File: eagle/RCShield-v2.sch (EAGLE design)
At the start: 48 parts, among them J1/J2 JOYSTICKPTH, U1 TOUSCRUINO_SHIELD, U2 FT232RL-BASICSSOP, U4 XBEE, X1 USBSMD

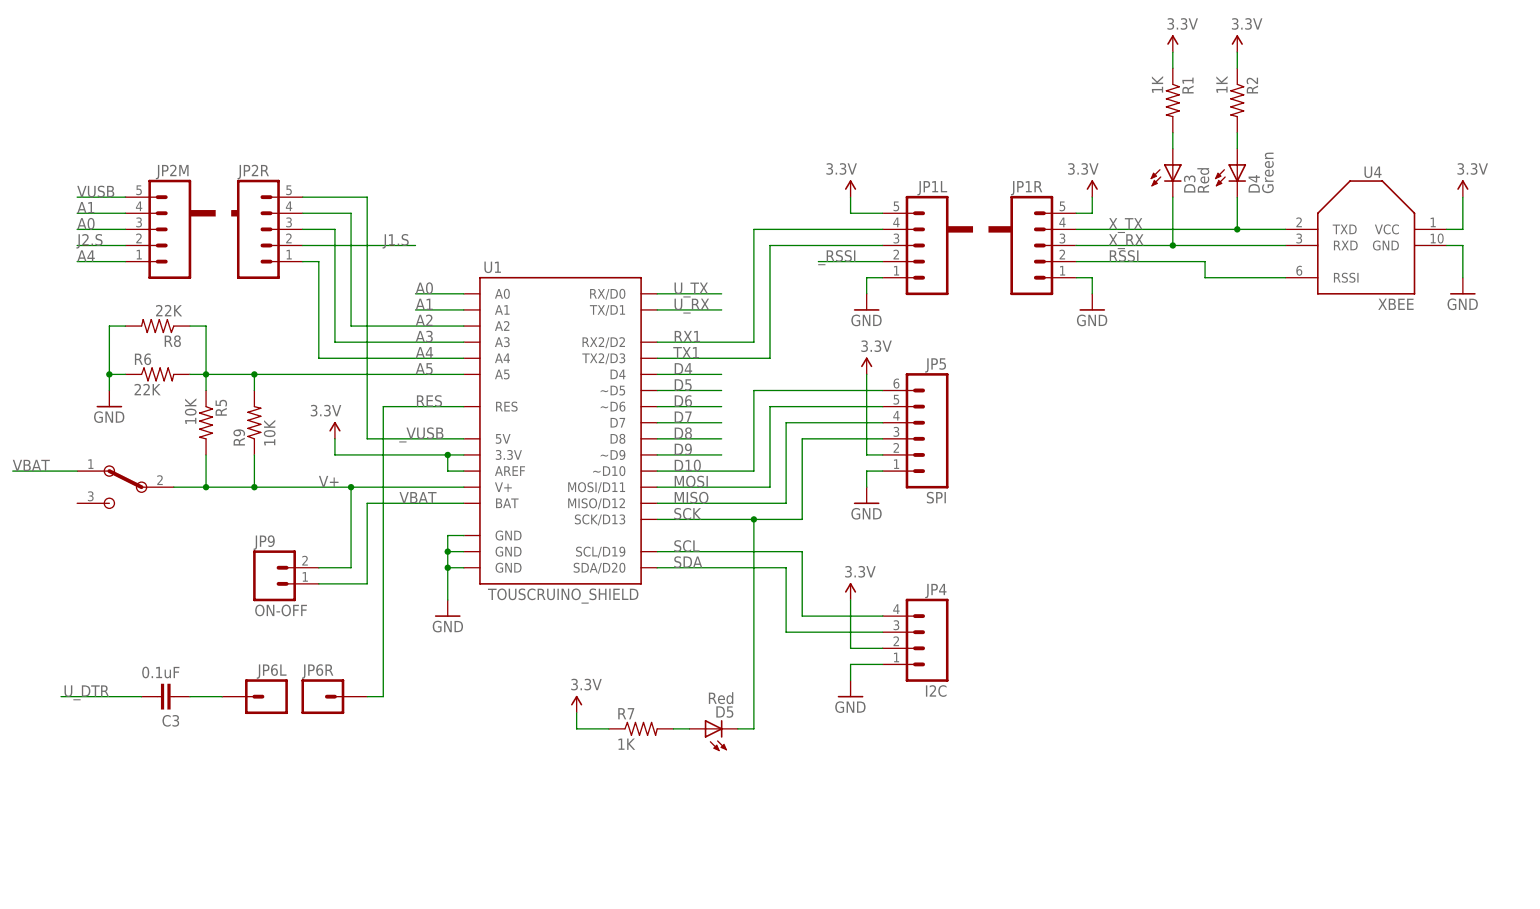
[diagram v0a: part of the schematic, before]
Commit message: 
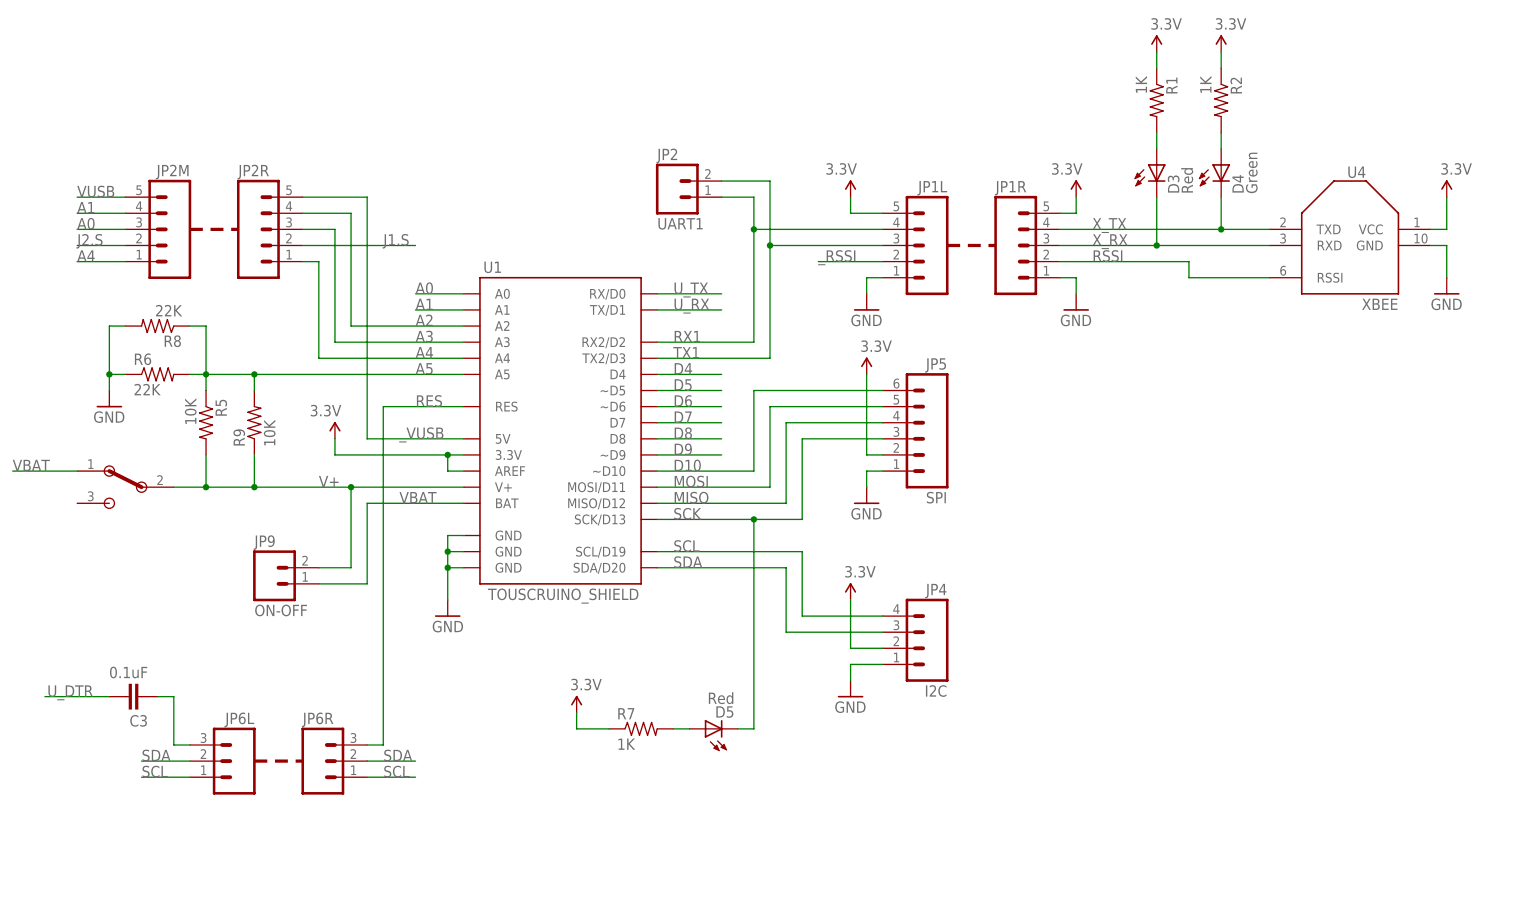
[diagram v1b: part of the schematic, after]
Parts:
- added JP2: UART1, wibauxl:M02
- JP6L, JP6R: value M01PTH -> (none); device SparkFun:M01PTH -> SparkFun:M03PTH
- P1/P3, P2/P4: value (none) -> POT; device SparkFun:POT -> wibauxl:POT
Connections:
- removed net N$11: C3.2, JP6L.1
- new net N$1: C3.2, JP6L.3
- net RES: now also JP6R.3; no longer JP6R.1
- net RX1: now also JP2.1
- net SCL: now also JP6L.1, JP6R.1
- net SDA: now also JP6L.2, JP6R.2
- net TX1: now also JP2.2
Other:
- moved on the sheet: C3, D3, D4, JP1R, R1, R2, U4

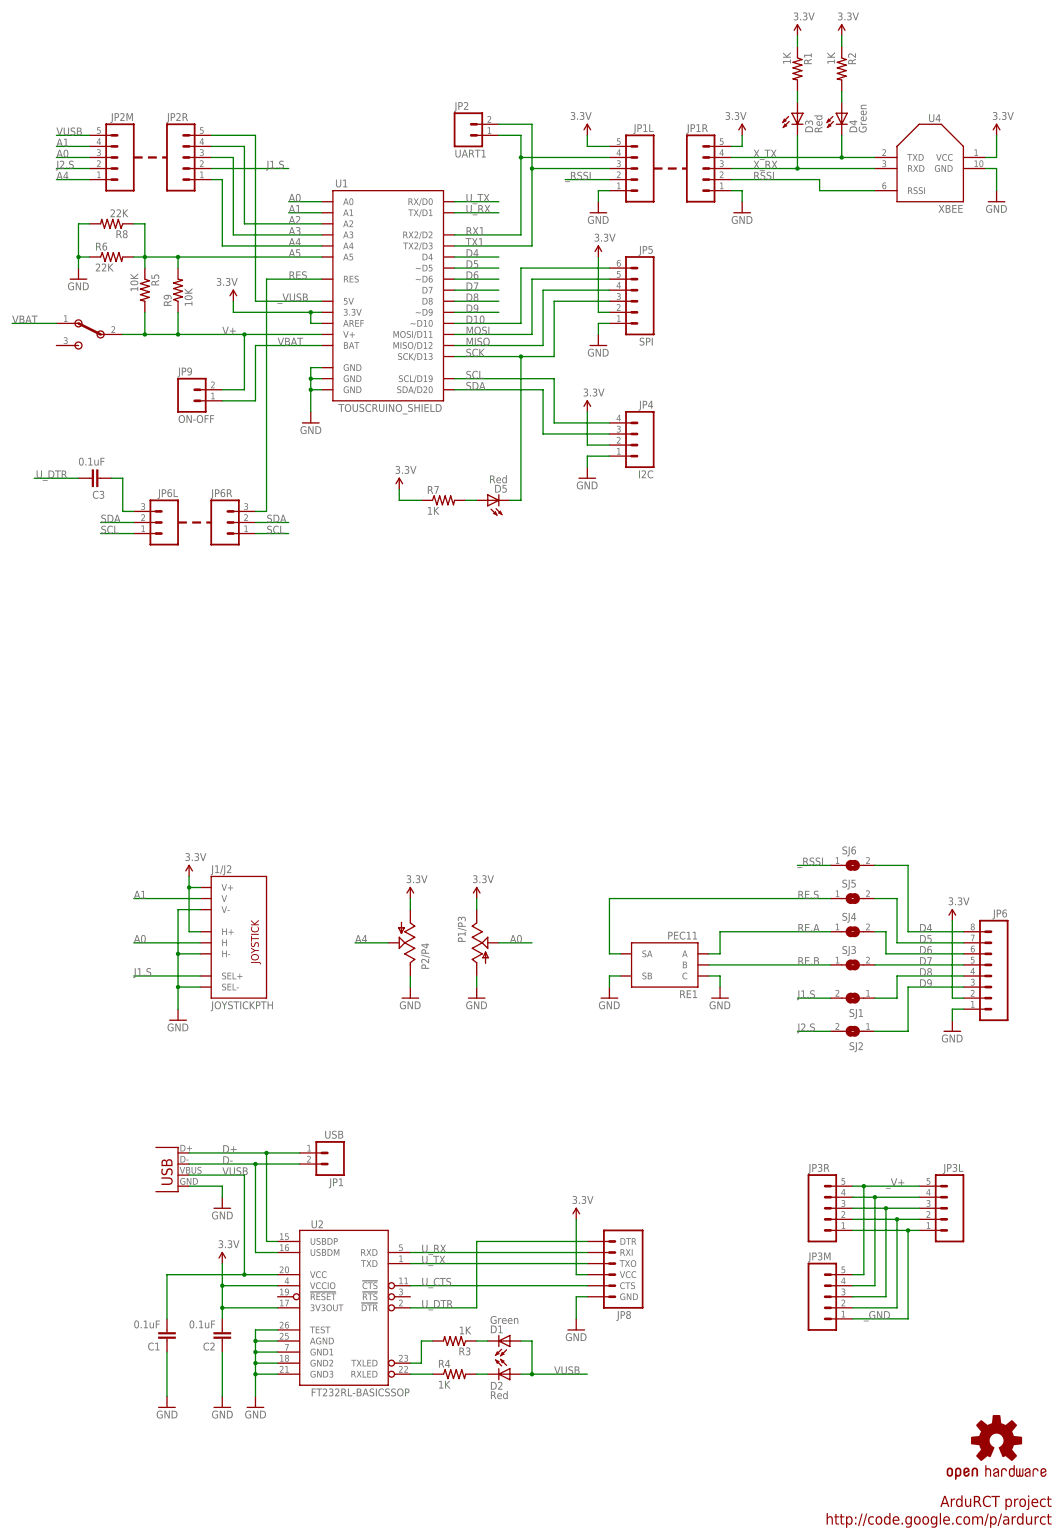
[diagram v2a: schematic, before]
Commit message: 
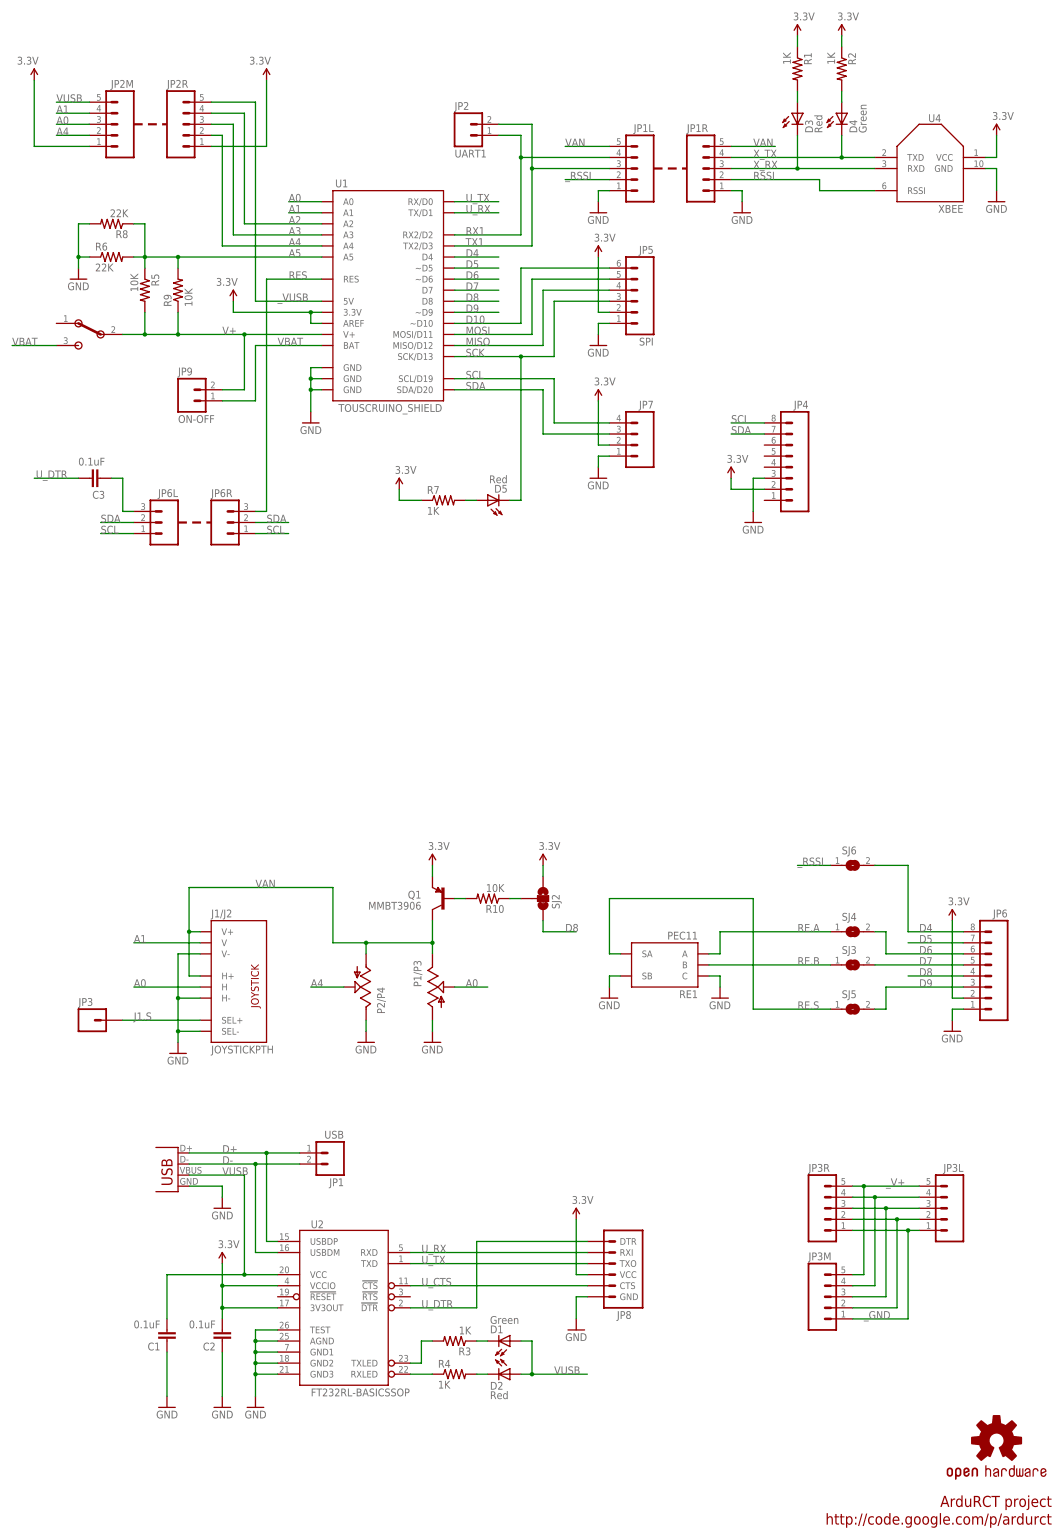
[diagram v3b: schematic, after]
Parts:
- removed SJ1: (no value), jumper:SJ
- added JP3: M01PTH, SparkFun:M01PTH
- added JP7: M04, wibauxl:M04
- added Q1: MMBT3906, wibauxl:TRANSISTOR_PNPSMD
- added R10: 10K, SparkFun:RESISTOR0805-RES
- JP4: value I2C -> M08; device wibauxl:M04 -> wibauxl:M08
- SJ2: value (none) -> SJ_2WAYS_1-2W; device jumper:SJ -> wibauxl:SJ_2WAYS_1-2W
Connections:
- removed net J2.S: JP2M.2, SJ2.2
- new net N$2: Q1.B, R10.2
- new net N$3: R10.1, SJ2.2
- new net VAN: J1/J2.H+, J1/J2.V+, JP1L.5, JP1R.5, P1/P3.E, P2/P4.A, Q1.C
- net 3.3V: now also JP2M.1, JP2R.1, JP7.2, Q1.E, SJ2.3; no longer J1/J2.H+, J1/J2.V+, JP1L.5, JP1R.5, P1/P3.E, P2/P4.A
- net A4: now also JP2M.2, JP2R.2; no longer JP2M.1, JP2R.1
- net D5: no longer SJ5.2
- net D8: now also SJ2.1; no longer SJ1.1
- net D9: now also SJ5.2; no longer SJ2.1
- net GND: now also JP4.3, JP7.1; no longer JP4.1
- net J1.S: now also JP3.1; no longer JP2R.2, SJ1.2
- net SCL: now also JP4.8, JP7.4; no longer JP4.4
- net SDA: now also JP4.7, JP7.3; no longer JP4.3
- net VBAT: now also S4.3; no longer S4.1
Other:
- moved on the sheet: J1/J2, JP2M, JP2R, P1/P3, P2/P4, SJ5

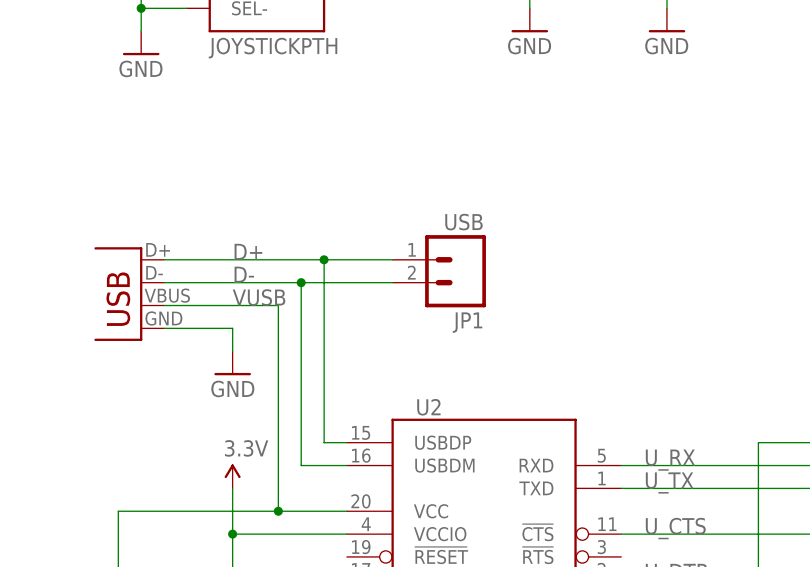
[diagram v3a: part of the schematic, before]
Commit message: 
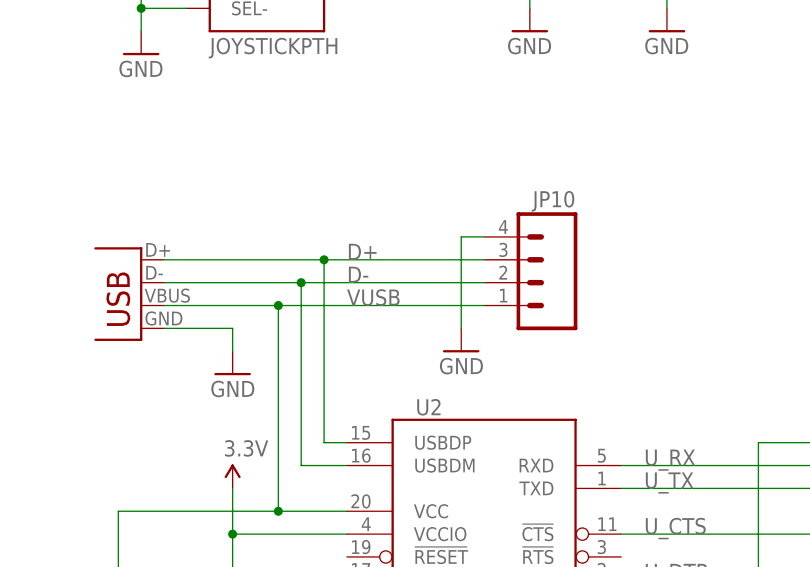
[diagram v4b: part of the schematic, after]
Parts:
- removed JP1: USB, wibauxl:M02
- added JP10: M04, wibauxl:M04
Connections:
- net D+: now also JP10.3; no longer JP1.1
- net D-: now also JP10.2; no longer JP1.2
- net GND: now also JP10.4
- net VUSB: now also JP10.1
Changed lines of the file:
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@@
 <part name="R9" library="resistor" deviceset="R-US_" device="0207/7" value="10K"/>
 <part name="P+15" library="SparkFun" deviceset="3.3V" device=""/>
-<part name="JP1" library="wibauxl" deviceset="M02" device="" value="USB"/>
 <part name="RE1" library="wibauxl" deviceset="PEC11" device=""/>
 <part name="U$4" library="wibauxl" deviceset="FRAME_LETTER" device=""/>
@@
 <part name="GND12" library="SparkFun" deviceset="GND" device=""/>
 <part name="P+4" library="SparkFun" deviceset="3.3V" device=""/>
+<part name="JP10" library="wibauxl" deviceset="M04" device="" value=""/>
+<part name="GND13" library="SparkFun" deviceset="GND" device=""/>
 </parts>
 <sheets>
@@
 <instance part="R9" gate="G$1" x="43.18" y="302.26" rot="R90"/>
 <instance part="P+15" gate="G$1" x="53.34" y="78.74"/>
-<instance part="JP1" gate="G$1" x="76.2" y="104.14" rot="R180"/>
 <instance part="RE1" gate="G$1" x="154.94" y="147.32" rot="MR0"/>
 <instance part="U$4" gate="G$1" x="0" y="210.82"/>
@@
 <instance part="GND12" gate="1" x="175.26" y="248.92"/>
 <instance part="P+4" gate="G$1" x="170.18" y="259.08"/>
+<instance part="JP10" gate="G$1" x="86.36" y="101.6" rot="MR0"/>
+<instance part="GND13" gate="1" x="78.74" y="93.98" rot="MR0"/>
 </instances>
 <busses>
@@
 <pinref part="GND12" gate="1" pin="GND"/>
 </segment>
+<segment>
+<pinref part="JP10" gate="G$1" pin="4"/>
+<wire x1="81.28" y1="106.68" x2="78.74" y2="106.68" width="0.1524" layer="91"/>
+<wire x1="78.74" y1="106.68" x2="78.74" y2="96.52" width="0.1524" layer="91"/>
+<pinref part="GND13" gate="1" pin="GND"/>
+</segment>
 </net>
 <net name="3.3V" class="0">
@@
 <wire x1="40.64" y1="76.2" x2="40.64" y2="66.04" width="0.1524" layer="91"/>
 <junction x="58.42" y="76.2"/>
-<label x="53.34" y="99.06" size="1.778" layer="95"/>
+<label x="66.04" y="99.06" size="1.778" layer="95"/>
 <pinref part="U2" gate="G$1" pin="VCC"/>
 <pinref part="X1" gate="G$1" pin="VBUS"/>
 <pinref part="C1" gate="G$1" pin="2"/>
+<pinref part="JP10" gate="G$1" pin="1"/>
+<wire x1="58.42" y1="99.06" x2="81.28" y2="99.06" width="0.1524" layer="91"/>
+<junction x="58.42" y="99.06"/>
 </segment>
 <segment>
@@
 <wire x1="63.5" y1="83.82" x2="63.5" y2="104.14" width="0.1524" layer="91"/>
 <wire x1="63.5" y1="104.14" x2="45.72" y2="104.14" width="0.1524" layer="91"/>
-<label x="53.34" y="104.14" size="1.778" layer="95"/>
+<label x="66.04" y="104.14" size="1.778" layer="95"/>
 <pinref part="U2" gate="G$1" pin="USBDP"/>
 <pinref part="X1" gate="G$1" pin="D+"/>
-<wire x1="63.5" y1="104.14" x2="71.12" y2="104.14" width="0.1524" layer="91"/>
-<pinref part="JP1" gate="G$1" pin="1"/>
+<wire x1="63.5" y1="104.14" x2="81.28" y2="104.14" width="0.1524" layer="91"/>
 <junction x="63.5" y="104.14"/>
+<pinref part="JP10" gate="G$1" pin="3"/>
 </segment>
 </net>
@@
 <wire x1="60.96" y1="81.28" x2="60.96" y2="101.6" width="0.1524" layer="91"/>
 <wire x1="60.96" y1="101.6" x2="45.72" y2="101.6" width="0.1524" layer="91"/>
-<label x="53.34" y="101.6" size="1.778" layer="95"/>
+<label x="66.04" y="101.6" size="1.778" layer="95"/>
 <pinref part="U2" gate="G$1" pin="USBDM"/>
 <pinref part="X1" gate="G$1" pin="D-"/>
-<wire x1="60.96" y1="101.6" x2="71.12" y2="101.6" width="0.1524" layer="91"/>
-<pinref part="JP1" gate="G$1" pin="2"/>
+<wire x1="60.96" y1="101.6" x2="81.28" y2="101.6" width="0.1524" layer="91"/>
 <junction x="60.96" y="101.6"/>
-</segment>
-</net>
+<pinref part="JP10" gate="G$1" pin="2"/>
+</segment>
+</net>
